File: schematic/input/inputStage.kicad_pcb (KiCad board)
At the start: 2 copper layers, 99.1 x 58.5 mm, 37 parts, among them IC1 LM361N_NOPB, IC2 ADA4891-2ARMZ-R7, J1 Screw_Terminal_01x04, J2 Screw_Terminal_01x04, U1 LM324, U2 LM7805_TO220

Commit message: Added small decoupling caps
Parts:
- added C12: 100nF, Capacitor_THT:C_Disc_D5.0mm_W2.5mm_P5.00mm, F.Cu at (78.3, 100.1)
- added C13: 100nF, Capacitor_THT:C_Disc_D5.0mm_W2.5mm_P5.00mm, F.Cu at (115.4, 116.5)
- added C14: 100nF, Capacitor_THT:C_Disc_D5.0mm_W2.5mm_P5.00mm, F.Cu at (102.2, 124.7)
- moved R2 7.91 mm to (70.7, 88.0)
- moved R11 6.50 mm to (68.2, 91.2)
- moved R13 6.50 mm to (68.1, 94.5)
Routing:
- net +5V: track 108.1 -> 124.9 mm
- net Net-(R11-Pad1): track 16.8 -> 26.6 mm
- net Net-(C1-Pad2): track 15.8 -> 22.5 mm
- net Bias: track 20.4 -> 26.9 mm
- net Vcc: track 76.8 -> 79.2 mm
- net Net-(R11-Pad2): track 9.03 -> 9.79 mm
- net Net-(C4-Pad1): track 36.5 -> 35.8 mm

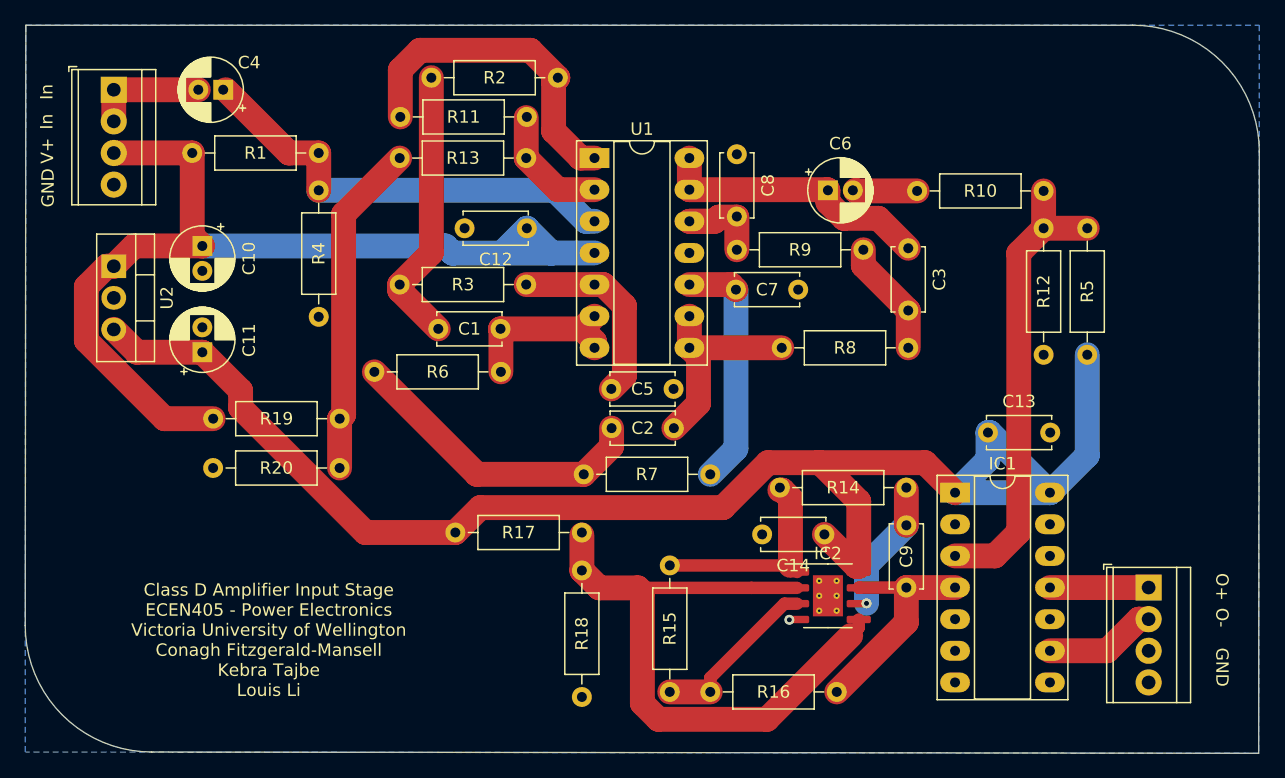
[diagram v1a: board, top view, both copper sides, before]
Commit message: Updated terminals and added IC labels
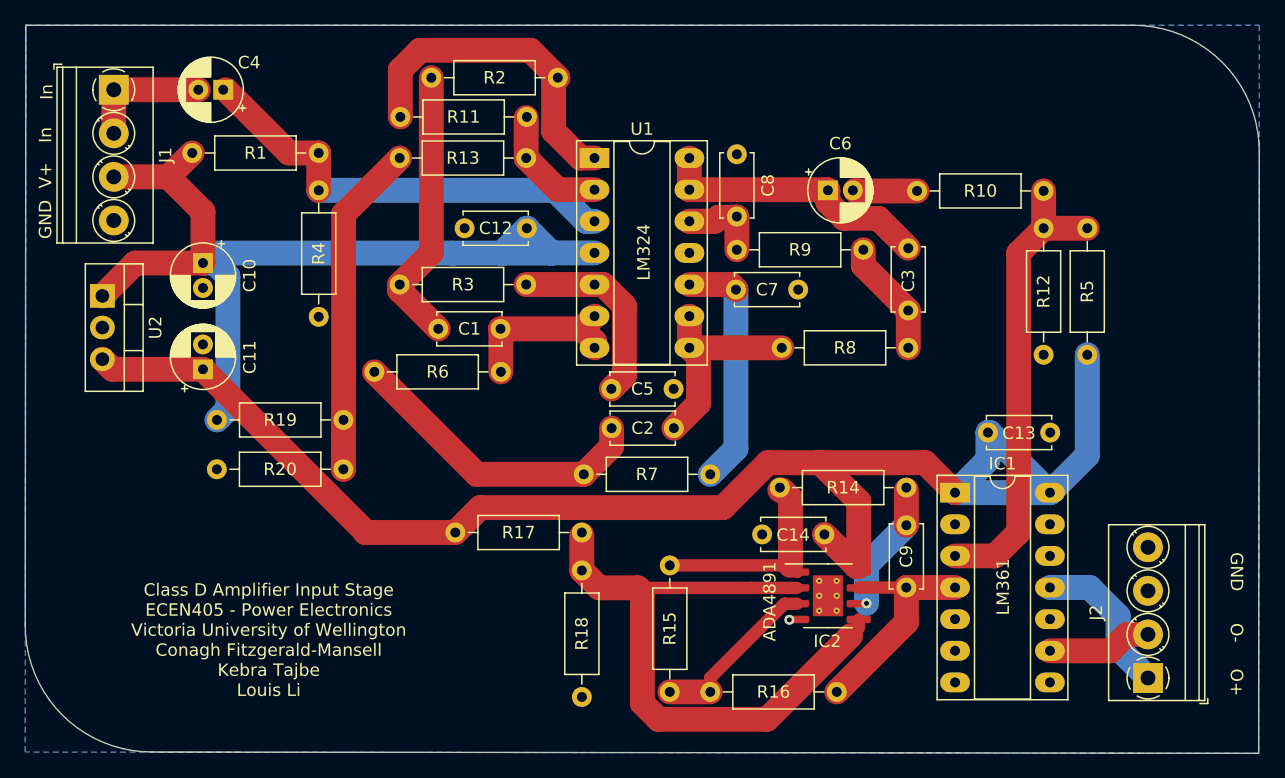
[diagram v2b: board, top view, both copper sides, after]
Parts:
- J1, J2: footprint TerminalBlock_TE-Connectivity:TerminalBlock_TE_282834-4_1x04_P2.54mm_Horizontal -> TerminalBlock_Phoenix:TerminalBlock_Phoenix_PT-1,5-4-3.5-H_1x04_P3.50mm_Horizontal
- moved J2 7.26 mm to (128.2, 136.2), turned to 90 degrees
- moved U2 2.56 mm to (44.2, 105.6)
- moved C10 1.37 mm to (52.3, 102.9)
- moved C11 1.37 mm to (52.3, 111.5)
- moved R19 0.32 mm to (53.4, 115.5)
- moved R20 0.32 mm to (63.6, 119.5)
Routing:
- net PWM+: track 7.92 -> 12.4 mm
- net Vcc: track 79.2 -> 76.1 mm
- net Input: track 9.33 -> 10.3 mm
- net +5V: track 124.9 -> 124.1 mm
- net PWM-: track 8.98 -> 8.42 mm
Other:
- board text added: "ADA4891"
- board text added: "LM324"
- board text added: "LM361"
